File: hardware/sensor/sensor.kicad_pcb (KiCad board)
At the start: 4 copper layers, 40 x 50 mm, 54 parts, among them J101 Conn_Coaxial, J201 PWR, J202 control signals, J203 GND, J204 LDO_{EN}, J205 V_{DD}AN, J206 V_{DD}MCU, J207 GND, J208 GND, J301 GND, J302 U_{ref}, J401 U_{SS}, J402 U_{DD}, J403 GND, J404 GND, J405 Out, J501 ADC, J502 GND, J503 toDefboard, J601 ISP, J602 IO, J603 LDO_{EN}, Q401 BC847BDW1, Q402 NMOS, SW601 SW_Push, U301 LTC2064, U601 nRF52810-QFxx, Y601 Crystal, Y602 Crystal_GND24

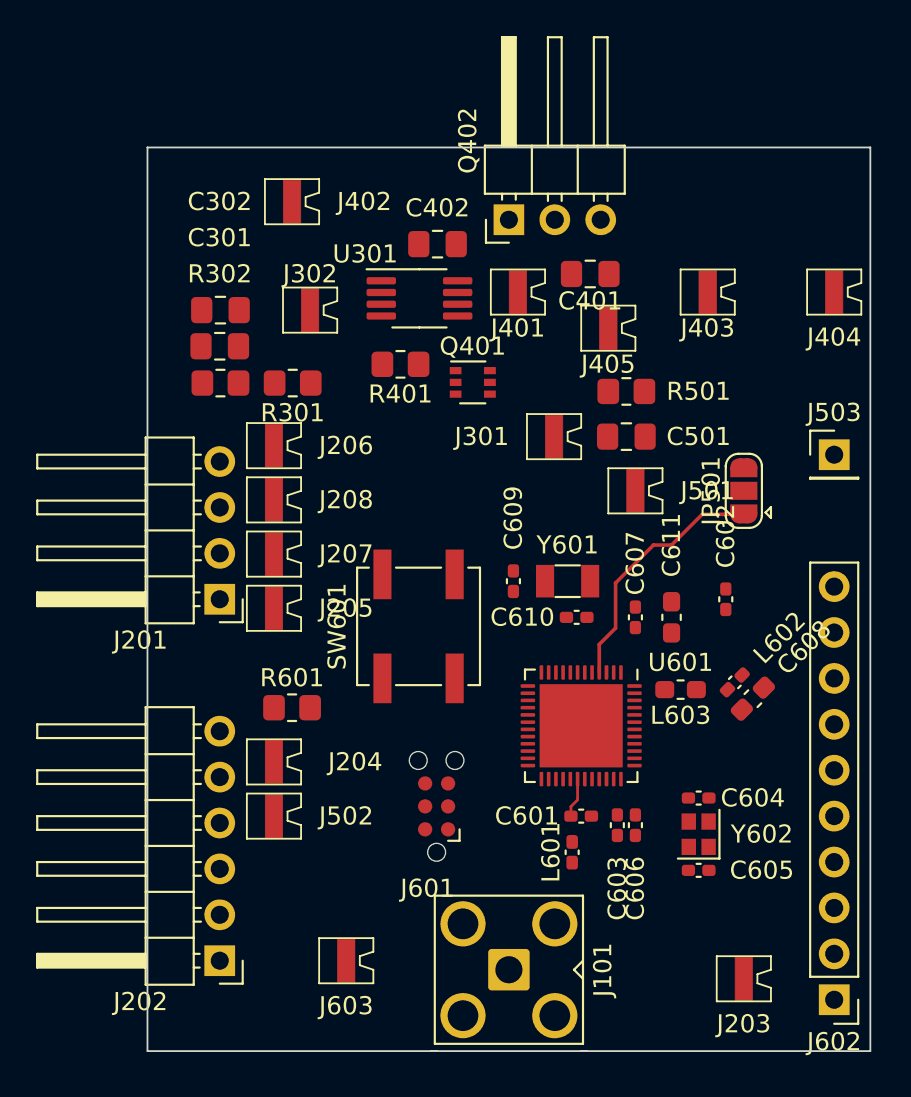
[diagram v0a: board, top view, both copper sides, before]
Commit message: Finished initial pcb routing
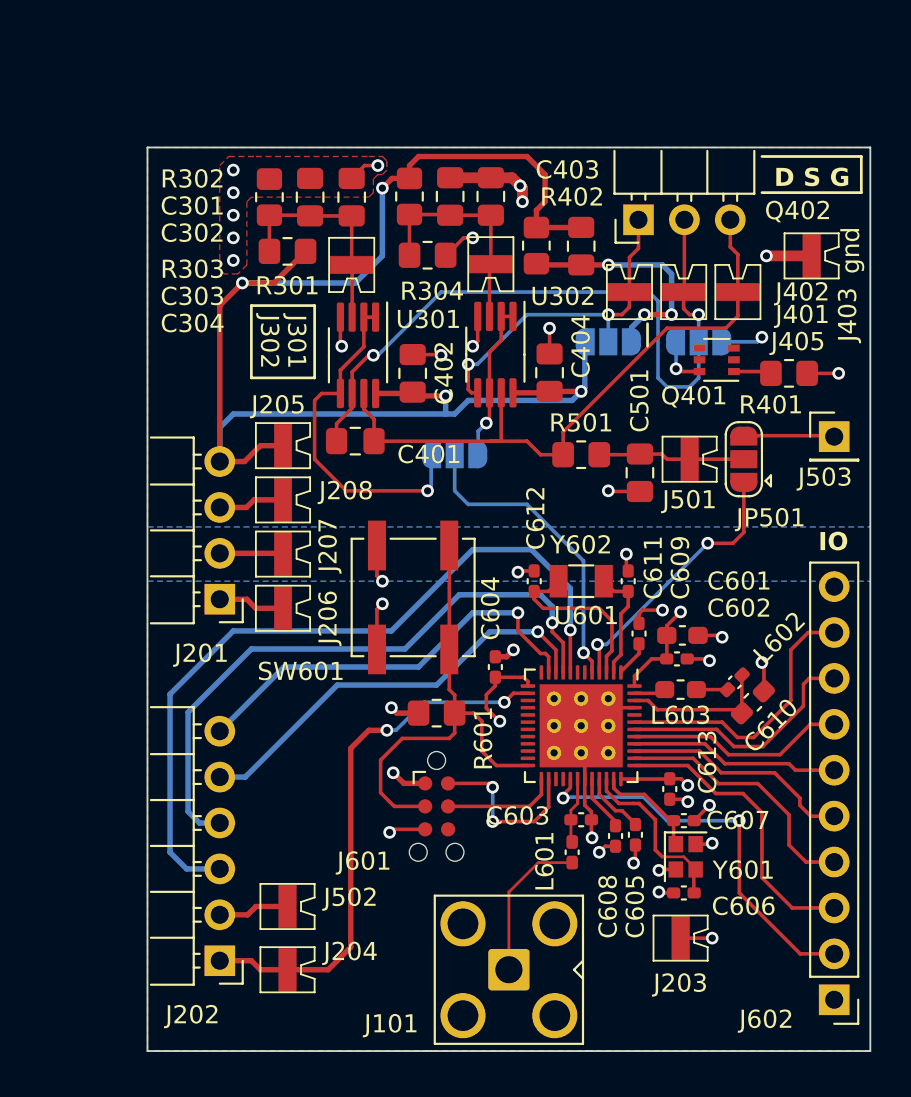
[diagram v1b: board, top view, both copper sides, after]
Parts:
- removed J404: GND, testpoint_519x:Testpoint_519xTR
- removed J603: LDO_{EN}, testpoint_519x:Testpoint_519xTR
- added C303: 100n, Capacitor_SMD:C_0805_2012Metric_Pad1.18x1.45mm_HandSolder, F.Cu at (128.8, 62.7)
- added C304: 10u, Capacitor_SMD:C_0805_2012Metric_Pad1.18x1.45mm_HandSolder, F.Cu at (131.0, 62.7)
- added C403: 10u, Capacitor_SMD:C_0805_2012Metric_Pad1.18x1.45mm_HandSolder, F.Cu at (136.0, 65.5)
- added C404: 100n, Capacitor_SMD:C_0805_2012Metric_Pad1.18x1.45mm_HandSolder, F.Cu at (134.2, 72.5)
- added C612: 12p, Capacitor_SMD:C_0402_1005Metric_Pad0.74x0.62mm_HandSolder, F.Cu at (133.4, 84.0)
- added C613: 100n, Capacitor_SMD:C_0402_1005Metric_Pad0.74x0.62mm_HandSolder, F.Cu at (140.9, 95.5)
- added JP301: J|T, Jumper:SolderJumper-3_P1.3mm_Open_RoundedPad1.0x1.5mm, B.Cu at (129.0, 77.0)
- added JP402: J|T, Jumper:SolderJumper-3_P1.3mm_Open_RoundedPad1.0x1.5mm, B.Cu at (142.5, 70.8)
- added JP403: J|T, Jumper:SolderJumper-3_P1.3mm_Open_RoundedPad1.0x1.5mm, B.Cu at (137.5, 70.8)
- added R303: R, Resistor_SMD:R_0805_2012Metric_Pad1.20x1.40mm_HandSolder, F.Cu at (126.5, 62.7)
- added R304: R, Resistor_SMD:R_0805_2012Metric_Pad1.20x1.40mm_HandSolder, F.Cu at (127.5, 66.0)
- added R402: 56k, Resistor_SMD:R_0805_2012Metric_Pad1.20x1.40mm_HandSolder, F.Cu at (133.5, 65.4)
- added U302: LTC2064, Package_SO:MSOP-8_3x3mm_P0.65mm, F.Cu at (131.2, 71.5)
- C601: value 0p8 -> 4u7; footprint Capacitor_SMD:C_0402_1005Metric_Pad0.74x0.62mm_HandSolder -> Capacitor_SMD:C_0603_1608Metric_Pad1.08x0.95mm_HandSolder
- C603: value 100p -> 0p8
- C604, C609: value 12p -> 100n
- C605: value 12p -> 100p
- C606: value DNP -> 12p
- C607: value 100n -> 12p
- C608: value 1u -> DNP; footprint Capacitor_SMD:C_0603_1608Metric_Pad1.08x0.95mm_HandSolder -> Capacitor_SMD:C_0402_1005Metric_Pad0.74x0.62mm_HandSolder
- C610: value 12p -> 1u; footprint Capacitor_SMD:C_0402_1005Metric_Pad0.74x0.62mm_HandSolder -> Capacitor_SMD:C_0603_1608Metric_Pad1.08x0.95mm_HandSolder
- C611: value 4u7 -> 12p; footprint Capacitor_SMD:C_0603_1608Metric_Pad1.08x0.95mm_HandSolder -> Capacitor_SMD:C_0402_1005Metric_Pad0.74x0.62mm_HandSolder
- J301: value GND -> U_{ref}
- U601: footprint Package_DFN_QFN:QFN-48-1EP_6x6mm_P0.4mm_EP4.6x4.6mm -> Package_DFN_QFN:QFN-48-1EP_6x6mm_P0.4mm_EP4.6x4.6mm_ThermalVias
- Y601: value Crystal -> Crystal_GND24; footprint Crystal:Crystal_SMD_3215-2Pin_3.2x1.5mm -> Crystal:Crystal_SMD_2016-4Pin_2.0x1.6mm
- Y602: value Crystal_GND24 -> Crystal; footprint Crystal:Crystal_SMD_2016-4Pin_2.0x1.6mm -> Crystal:Crystal_SMD_3215-2Pin_3.2x1.5mm
- moved R401 21.5 mm to (147.5, 72.5), turned to 0 degrees
- moved J402 20.1 mm to (139.7, 68.0), turned to 90 degrees
- moved Y601 16.6 mm to (141.8, 99.2), turned to -90 degrees
- moved C401 16.0 mm to (123.5, 76.2)
- moved Y602 15.4 mm to (136.0, 84.0), turned to 180 degrees
- moved Q401 13.6 mm to (143.5, 71.8), turned to 180 degrees
- moved C604 13.4 mm to (131.2, 88.8), turned to 90 degrees
- moved C607 11.6 mm to (141.7, 97.2), turned to 0 degrees
- moved J204 11.5 mm to (119.8, 106.5)
- moved C601 11.5 mm to (141.6, 87.0)
- moved J301 11.5 mm to (130.0, 66.5), turned to -90 degrees
- moved C610 10.8 mm to (145.5, 90.7), turned to 45 degrees
- moved C608 10.7 mm to (137.9, 98.1), turned to -90 degrees
- moved R302 10.6 mm to (118.8, 62.8), turned to 90 degrees
- moved J401 10.2 mm to (142.7, 68.0), turned to 90 degrees
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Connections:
- C601 pad 1: /Microcontroller/rf_out -> /Microcontroller/V_{DD}
- C603 pad 1: Net-(U601-DEC3) -> /Microcontroller/rf_out
- C604 pad 1: /Microcontroller/osc_xc1 -> /Microcontroller/V_{DD}
- C605 pad 1: /Microcontroller/osc_xc2 -> Net-(U601-DEC3)
- C606 pad 1: Net-(U601-DEC2) -> /Microcontroller/osc_xc1
- C607 pad 1: Net-(U601-DEC1) -> /Microcontroller/osc_xc2
- C608 pad 1: /Microcontroller/dcdc_dec4 -> Net-(U601-DEC2)
- C609 pad 1: /Microcontroller/osc_xl1 -> Net-(U601-DEC1)
- C610 pad 1: /Microcontroller/osc_xl2 -> /Microcontroller/dcdc_dec4
- C611 pad 1: /Microcontroller/V_{DD} -> /Microcontroller/osc_xl1
- J201 pad 1: /P_{IN}/LDO_{OUT} -> /Microcontroller/V_{DD}
- J201 pad 4: /Microcontroller/V_{DD} -> /P_{IN}/LDO_{OUT}
- J202 pad 1: /P_{IN}/PWG-LDO -> /Microcontroller/LDO_{EN}
- J202 pad 2: /P_{IN}/PWG-Vout -> GND
- J202 pad 3: /P_{IN}/EH-ON -> /P_{IN}/HBO-MCU
- J202 pad 4: /P_{IN}/HBO-MCU -> /P_{IN}/EH-ON
- J202 pad 5: GND -> /P_{IN}/PWG-Vout
- J202 pad 6: /Microcontroller/LDO_{EN} -> /P_{IN}/PWG-LDO
- J301 pad 1: GND -> Net-(J301-Pin_1)
- J402 pad 1: /P_{IN}/LDO_{OUT} -> Net-(J402-Pin_1)
- Q401 pad 2: /Microcontroller/V_{ref} -> /Sensor/V_{ref}
- Q401 pad 6: Net-(J401-Pin_1) -> Net-(JP402-A)
- Q402 pad 1: /P_{IN}/LDO_{OUT} -> Net-(J402-Pin_1)
- U301 pad 1: /Microcontroller/V_{ref} -> /Reference/ref_1v1
- U301 pad 2: /Microcontroller/V_{ref} -> /Reference/ref_1v1
- U301 pad 5: /Microcontroller/V_{ref} -> /Reference/ref_1v1
- U601 pad 10: /P_{IN}/EH-ON -> /P_{IN}/PWG-Vout
- U601 pad 11: /P_{IN}/HBO-MCU -> /P_{IN}/PWG-LDO
- U601 pad 8: /P_{IN}/PWG-LDO -> /P_{IN}/HBO-MCU
- U601 pad 9: /P_{IN}/PWG-Vout -> /P_{IN}/EH-ON
- Y601 pad 1: /Microcontroller/osc_xl2 -> /Microcontroller/osc_xc2
- Y601 pad 2: /Microcontroller/osc_xl1 -> GND
- Y602 pad 1: /Microcontroller/osc_xc2 -> /Microcontroller/osc_xl2
- Y602 pad 2: GND -> /Microcontroller/osc_xl1
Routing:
- net /P_{IN}/LDO_{OUT}: track 0.00 -> 81.1 mm, vias 0 -> 4
- net GND: track 0.00 -> 69.3 mm, vias 0 -> 36
- net /P_{IN}/HBO-MCU: track 0.00 -> 42.9 mm, vias 0 -> 1
- net Net-(J401-Pin_1): track 0.00 -> 39.5 mm, vias 0 -> 2
- net /Filter/In: track 0.00 -> 36.0 mm
- net /P_{IN}/EH-ON: track 0.00 -> 34.5 mm, vias 0 -> 1
- net /Microcontroller/LDO_{EN}: track 0.00 -> 30.0 mm, vias 0 -> 2
- net /Microcontroller/swd_rst: track 0.00 -> 26.0 mm
- net /P_{IN}/PWG-Vout: track 0.00 -> 23.6 mm, vias 0 -> 1
- net /P_{IN}/PWG-LDO: track 0.00 -> 23.4 mm, vias 0 -> 1
- net /Microcontroller/io_p024: track 0.00 -> 22.2 mm, vias 0 -> 2
- net /Microcontroller/V_{DD}: track 0.00 -> 21.9 mm, vias 0 -> 5
- net /Reference/ref_1v1: track 0.00 -> 19.3 mm, vias 0 -> 1
- net Net-(J402-Pin_1): track 0.00 -> 18.8 mm, vias 0 -> 2
- net /Microcontroller/V_{ref}: track 0.00 -> 17.1 mm, vias 0 -> 1
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- added copper zone on B.Cu, net /Microcontroller/V_{DD}
- added copper zone on B.Cu, net /P_{IN}/LDO_{OUT}
- added copper zone on F.Cu, net GND
- added copper zone on In1.Cu, net GND
- added copper zone on In2.Cu, net GND
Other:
- outline, holes or cut-outs redrawn
- board text added: "D S G"
- board text added: "ID:"
- board text added: "IO"
- board text added: "TychoJ Rev 1.0 05/jan/2024"
- board text added: "gnd"
- board text added: "pH sensor PCB"
